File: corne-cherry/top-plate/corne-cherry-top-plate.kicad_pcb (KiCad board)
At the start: 2 copper layers, 132.9 x 91.4 mm, 5 parts

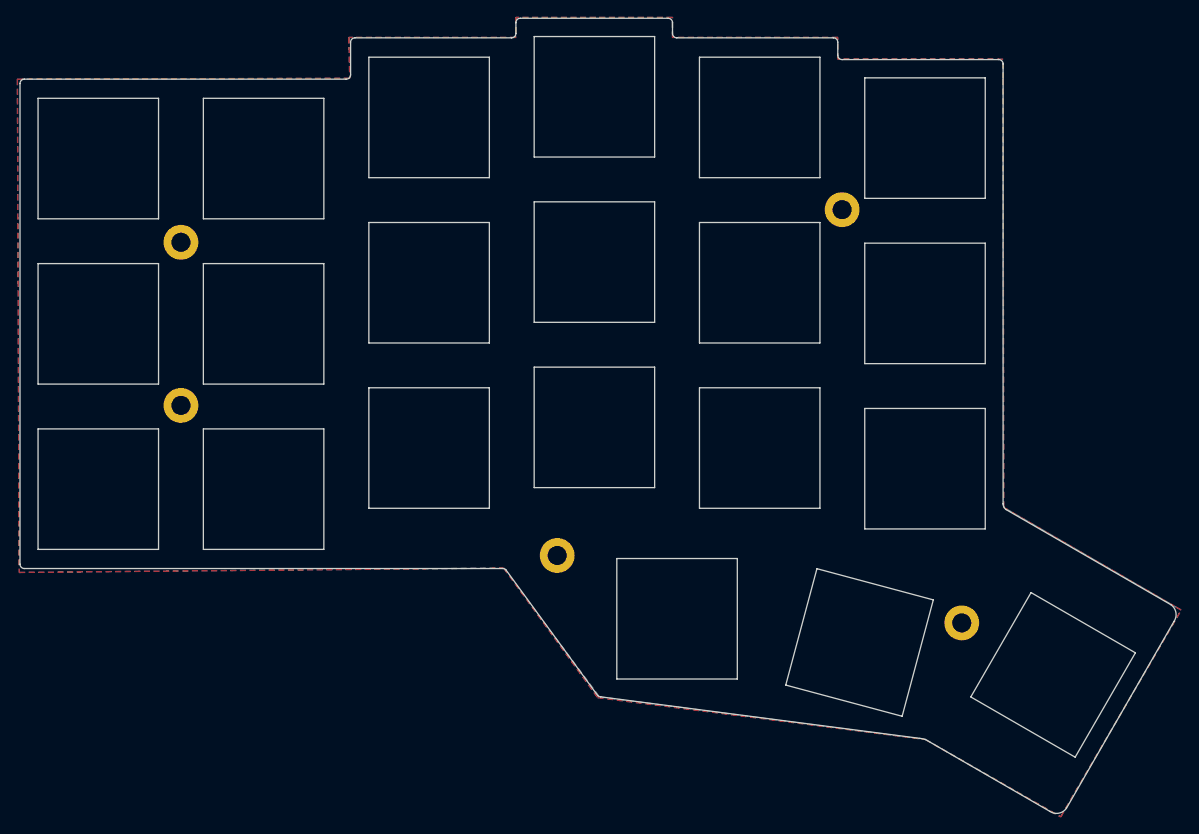
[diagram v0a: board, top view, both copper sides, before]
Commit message: Update switch hole size and gnd pattern
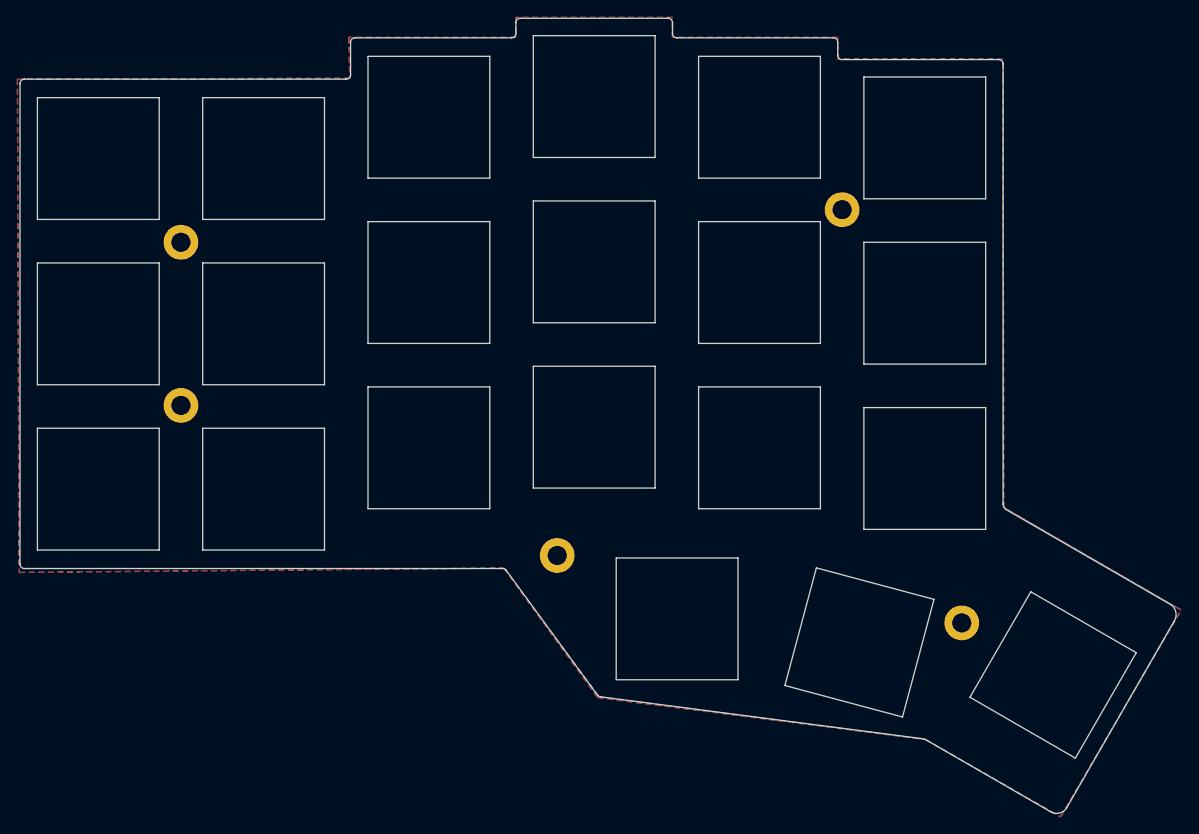
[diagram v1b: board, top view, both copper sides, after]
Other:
- outline, holes or cut-outs redrawn
- board text added: "Corne Cherry v2.1 PCB Designed by foostan"
- board text removed: "Corne Cherry v2.0 PCB Designed by foostan"

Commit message: Fix version
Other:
- board text added: "Corne Cherry v2.0 PCB Designed by foostan"
- board text removed: "Corne Cherry v2.1 PCB Designed by foostan"
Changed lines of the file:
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@@
     (title "Corne Cherry")
     (date 2018-11-15)
-    (rev 2.1)
+    (rev 2.0)
     (company foostan)
   )
@@
   (gr_line (start 79.5 105.5) (end 79.51 105.5) (angle 90) (layer Eco2.User) (width 2.5))
   (gr_line (start 79.5 86.75) (end 79.51 86.75) (angle 90) (layer Eco2.User) (width 2.5))
-  (gr_text "Corne Cherry v2.1\nPCB Designed by foostan" (at 117.55 121.45) (layer B.Mask)
+  (gr_text "Corne Cherry v2.0\nPCB Designed by foostan" (at 117.55 121.45) (layer B.Mask)
     (effects (font (size 1 1) (thickness 0.125)) (justify left mirror))
   )
-  (gr_text "Corne Cherry v2.1\nPCB Designed by foostan" (at 98.25 121.45) (layer F.Mask)
+  (gr_text "Corne Cherry v2.0\nPCB Designed by foostan" (at 98.25 121.45) (layer F.Mask)
     (effects (font (size 1 1) (thickness 0.125)) (justify left))
   )

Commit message: Update top-plate
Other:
- board text added: "Corne Keyboard v2.1 PCB Designed by foostan"
- board text removed: "Corne Cherry v2.0 PCB Designed by foostan"
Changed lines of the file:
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@@
   (page A4)
   (title_block
-    (title "Corne Cherry")
-    (date 2018-11-15)
-    (rev 2.0)
+    (title "Corne Keyboard")
+    (date 2018-12-09)
+    (rev 2.1)
     (company foostan)
   )
@@
   (gr_line (start 79.5 105.5) (end 79.51 105.5) (angle 90) (layer Eco2.User) (width 2.5))
   (gr_line (start 79.5 86.75) (end 79.51 86.75) (angle 90) (layer Eco2.User) (width 2.5))
-  (gr_text "Corne Cherry v2.0\nPCB Designed by foostan" (at 117.55 121.45) (layer B.Mask)
+  (gr_text "Corne Keyboard v2.1\nPCB Designed by foostan" (at 117.55 121.45) (layer B.Mask)
     (effects (font (size 1 1) (thickness 0.125)) (justify left mirror))
   )
-  (gr_text "Corne Cherry v2.0\nPCB Designed by foostan" (at 98.25 121.45) (layer F.Mask)
+  (gr_text "Corne Keyboard v2.1\nPCB Designed by foostan" (at 98.25 121.45) (layer F.Mask)
     (effects (font (size 1 1) (thickness 0.125)) (justify left))
   )
